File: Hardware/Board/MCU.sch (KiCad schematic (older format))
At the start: 65 parts, among them IC1 MX25LM51245GXDI00, IC2 IS66WVH8M8BLL-100B1LI_0, IC3 TSC2007, J14 52271-0679, J22 Conn_02x06_Odd_Even, J23 Conn_02x25_Odd_Even, J3 USB_B_Micro, J4 54104-4031, J5 Conn_ARM_JTAG_SWD_20, SW1 SW_Push, SW2 SW_Push, SW3 SW_Push, U17 STM32L4R9ZITx, U18 USBLC6-2SC6, U19 MOD-nRF8001, Y1 16MHz, Y2 32.768

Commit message: Alle Footprints definiert, Libs angepasst, Layout gestartet mit Plazierung, Controller und Breakout Netzmäßig getrennt.
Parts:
- removed Y1: 16MHz, symbol Device:Crystal
- added J24: Conn_01x06, Connector_PinHeader_2.54mm:PinHeader_1x06_P2.54mm_Vertical, symbol Connector_Generic:Conn_01x06
- added Y1: 16 MHz, Crystal:Crystal_SMD_3225-4Pin_3.2x2.5mm, symbol Device:Crystal_GND24
- SW1: value SW_Push -> Reset; footprint (none) -> Button_Switch_THT:SW_PUSH_6mm
- SW2: value SW_Push -> Boot; footprint (none) -> Button_Switch_THT:SW_PUSH_6mm
- SW3: value SW_Push -> Wakeup; footprint (none) -> Button_Switch_THT:SW_PUSH_6mm_H8.5mm
- Y2: footprint (none) -> Crystal:Crystal_SMD_MicroCrystal_CC7V-T1A-2Pin_3.2x1.5mm
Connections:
- net labels added: *LCD_BL_CTR, +3.3VP, PA9, PD13, PD4, PD7, VCC, VCCQ
- net labels removed: *PA9, +3.3V, +3.3VA, +VSW, GND, I2C2_SCL, I2C2_SDA, LCD_BL_CTR, LCD_BL_CTRL, LCD_LED-A, LCD_LED-K
- wire segments 514 -> 524

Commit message: Kleinigkeiten
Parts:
- IC3: symbol opendous:TSC2007 -> Womo-rescue:TSC2007-opendous

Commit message: Komplete enummerierung Geändert, Schaltplan zusammengefasst, Layout nochmals reset. BOM zu 75% fertig gestellt
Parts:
- C17: renamed from C78; footprint Capacitor_SMD:C_0603_1608Metric -> Capacitor_SMD:C_1210_3225Metric
- J5: renamed from J24; value Conn_01x06 -> Spare
- renumbered C4 to C1, C9 to C10, C10 to C11, C11 to C12, C79 to C13, C75 to C14, C76 to C15, C77 to C16, C70 to C18, C1 to C19, C5 to C2, C97 to C20, C2 to C21, C3 to C22, C12 to C23, C13 to C24, C83 to C25, C15 to C26, C98 to C27, C80 to C28, C81 to C29, C6 to C3, C82 to C30, C84 to C31, C85 to C32, C86 to C33, C100 to C34, C99 to C35, C101 to C36, C102 to C37, C7 to C4, C8 to C5, C71 to C6, C72 to C7, C73 to C8, C74 to C9, D19 to D1, FB45 to FB1, FB46 to FB2, FB49 to FB3, FB47 to FB4, FB48 to FB5, J23 to J1, J4 to J2, J14 to J3, J22 to J4, J3 to J6, J5 to J7, R75 to R1, R76 to R2, R77 to R3, R78 to R4, SW2 to SW1, SW3 to SW2, SW1 to SW3, U17 to U1, U18 to U2, U19 to U3

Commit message: Änderung des Konzeptes auf 2 Boards, eines TFT Touch mit STM32L4R9, das rein die Bedienung macht. Control Board mit STM32L476, mit noch mehr Schnittstellen. Bus zwischen Display, Board, Raspberry/ESP ist RS485, Bus als RJ45 mit Wakeup und Stromversorgung
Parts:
- removed C25, C26, C35, C36, C37: 1uF, Capacitor_SMD:C_0603_1608Metric, symbol Device:C
- removed FB1, FB2, FB3, FB4, FB5: Ferrite, Inductor_SMD:L_0603_1608Metric, symbol Device:Ferrite_Bead_Small
- removed IC3: TSC2007, Package_SO:TSSOP-16_4.4x5mm_P0.65mm, symbol Womo-rescue:TSC2007-opendous
- removed J1: Conn_02x25_Odd_Even, Connector_PinHeader_2.54mm:PinHeader_2x25_P2.54mm_Vertical, symbol Connector_Generic:Conn_02x25_Odd_Even
- removed J2: 54104-4031, SamacSys_Parts:54104-4031, symbol Womo-rescue:54104-4031-SamacSys_Parts
- removed J3: 52271-0679, SamacSys_Parts:52271-0679, symbol Womo-rescue:52271-0679-SamacSys_Parts
- removed J4: Conn_02x06_Odd_Even, Connector_PinHeader_2.54mm:PinHeader_2x06_P2.54mm_Vertical, symbol Connector_Generic:Conn_02x06_Odd_Even
- removed J5: Spare, Connector_PinHeader_2.54mm:PinHeader_1x06_P2.54mm_Vertical, symbol Connector_Generic:Conn_01x06
- removed U1: STM32L4R9ZITx, Package_QFP:LQFP-144_20x20mm_P0.5mm, symbol MCU_ST_STM32L4+:STM32L4R9ZITx
- added C?: 100nF, Capacitor_SMD:C_0603_1608Metric, symbol Device:C
- added U?: STM32L476ZGTx, Package_QFP:LQFP-144_20x20mm_P0.5mm, symbol MCU_ST_STM32L4:STM32L476ZGTx
- added U?: MAX3072E, Package_SO:SOIC-8_3.9x4.9mm_P1.27mm, symbol Interface_UART:MAX3072E
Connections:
- net labels added: +3.3V, CTRL_A, CTRL_B, GND, LIN_SEL_A0, LIN_SEL_A1, LIN_SEL_EN, SER_SEL_A0, SER_SEL_A1, SER_SEL_EN, SPI2_MISO, SPI2_MOSI, SPI2_NSS, SPI2_SCK, USART1_RTS_CTRL, USART1_RTS_DE_CTRL, USART1_RX_CTRL, USART1_TX_CTRL, USART2_RX_LIN, USART2_TX_LIN, USART3_RX_SER, USART3_TX_SER
- net labels removed: *LCD_BL_CTR, *LCD_LED-A, *LCD_LED-K, *PWR_Reset, *USART1_RX_LIN1, *USART1_TX_LIN1, *USART2_RX_LIN2, *USART2_TX_LIN2, *USART3_RX_LIN3, *USART3_TX_LIN3, LCD_37, LCD_38, LCD_39, LCD_40, LCD_B0, LCD_B1, LCD_B2, LCD_B3, LCD_B4, LCD_B5, LCD_B6, LCD_B7, LCD_CLK, LCD_DE, LCD_EN, LCD_G0, LCD_G1, LCD_G2, LCD_G3, LCD_G4, LCD_G5, LCD_G6, LCD_G7, LCD_HSYNC, LCD_INT, LCD_R0, LCD_R1, LCD_R2, LCD_R3, LCD_R4, LCD_R5, LCD_R6, LCD_R7, LCD_VSYNC, PD4, TOUCH_RESET, X+, X-, Y+, Y-
- wire segments 524 -> 349
- no-connect marks 23 -> 18
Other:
- note removed: "Connection to Mainboard"
- note removed: "I2C ADR: 1001000"
- note removed: "Touchconfig"
- note removed: "Touchcontroller"
- note removed: "Touchdisplay RGB TFT"
- moved on the sheet: C21, C22, Y1

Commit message: Display Unit Lib Fehler behoben, und noch Zeug raus geworfen Library jetzt projekt spezifisch im Hardware root.. Hauptplatine rund um den Prozessor a bissl was getan, vorbereitung Quadspi Flash und SD Karte.
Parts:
- removed IC1: MX25LM51245GXDI00, SamacSys_Parts:BGA24C100P5X5_600X800X35, symbol Womo-rescue:MX25LM51245GXDI00-SamacSys_Parts
- removed IC2: IS66WVH8M8BLL-100B1LI_0, SamacSys_Parts:BGA24C100P5X5_600X800X35, symbol Womo-rescue:IS66WVH8M8BLL-100B1LI_0-SamacSys_Parts
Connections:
- net labels added: 3VA_EN, 5V_EN, 5V_GSM_EN, 5V_Raspi_EN, CAN1_RX, CAN1_TX, I2C2_SCL, I2C2_SDA, LPUART_RTS_DE_RS485, LPUART_RX_RX485, LPUART_TX_RS485, QSPI_D0, QSPI_D1, QSPI_D2, QSPI_D3, QSPI_NCS, QSPI_SCK, Rasp_Shutdown, Rasp_down, UART5_RX, UART5_TX, uSD_CLK, uSD_D0, uSD_D1, uSD_D2, uSD_D3, uSD_Detect
- net labels removed: *CAN1_RX, *CAN1_TX, *I2C2_SCL, *I2C2_SDA, *LPUART_RTS_DE_RS485, *LPUART_RX_RX485, *LPUART_TX_RS485, *PB2, *PC6, *PC7, *Rasp_Shutdown, *Rasp_down, *UART5_RX, *UART5_TX, OctoSPI_P1_CLK, OctoSPI_P1_DQS, OctoSPI_P1_IO0, OctoSPI_P1_IO1, OctoSPI_P1_IO2, OctoSPI_P1_IO3, OctoSPI_P1_IO4, OctoSPI_P1_IO5, OctoSPI_P1_IO6, OctoSPI_P1_IO7, OctoSPI_P1_NCS, OctoSPI_P2_CLK, OctoSPI_P2_DQS, OctoSPI_P2_IO0, OctoSPI_P2_IO1, OctoSPI_P2_IO2, OctoSPI_P2_IO3, OctoSPI_P2_IO4, OctoSPI_P2_IO5, OctoSPI_P2_IO6, OctoSPI_P2_IO7, OctoSPI_P2_NCS, PD13, PD7, TOUCH_INT
- wire segments 349 -> 295
- no-connect marks 18 -> 6
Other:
- moved on the sheet: C23, C24, C27, R3, R4, Y2

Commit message: Alle Busse aus dem Prozessor geroutet, Multplexing der LIN, RS485 und TTY Busse, diverse Aufräumarbeiten.
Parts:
- removed C28, C29, C31, C32, C33, C?: 100nF, Capacitor_SMD:C_0603_1608Metric, symbol Device:C
- removed U?: MAX3072E, Package_SO:SOIC-8_3.9x4.9mm_P1.27mm, symbol Interface_UART:MAX3072E
- added C? (x2): 100nF, Capacitor_SMD:C_0603_1608Metric, symbol Device:C
- added FB? (x2): 100R, Inductor_SMD:L_0603_1608Metric, symbol Device:Ferrite_Bead_Small
- added J?: SD_Card, symbol Connector:SD_Card
- added R? (x6): 47K, Resistor_SMD:R_0603_1608Metric, symbol Device:R
- added U?: TJA1049T-3, Package_SO:SOIC-8_3.9x4.9mm_P1.27mm, symbol Interface_CAN_LIN:TJA1049T-3
- added U?: M25Q128A, Package_SO:SOIJ-8_5.3x5.3mm_P1.27mm, symbol Memory_Flash:M25PX32-VMW
- C23, C24: value 3p3 -> 4p7
- Y1: value 16 MHz -> 25 MHz
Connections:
- net labels added: +3.3VA, +5V, CTRL_H, CTRL_L, I2C1_SCL, I2C1_SDA, QSPI_CLK, RS485_SEL_A0, RS485_SEL_A1, RS485_SEL_EN, SLP-LIN1, SLP-LIN2, SLP-LIN3, SLP-LIN4, SPI3_MISO, SPI3_MOSI, SPI3_NSS, SPI3_SCK, STB-CAN, STB-CTRL, UART4_RX_GSM, UART4_TX_GSM, uSD_CMD
- net labels removed: *I2C4_SCL, *I2C4_SDA, *PF11, *UART4_RX, *UART4_TX, +3.3VP, CTRL_A, CTRL_B, PA9, QSPI_SCK, UART5_RX, UART5_TX, USART1_RTS_CTRL, USART1_RTS_DE_CTRL, VCC, VCCQ
- wire segments 295 -> 332
- no-connect marks 6 -> 2
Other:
- moved on the sheet: C1, C10, C11, C12, C13, C14, C15, C16, C17, C2, C20, C27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

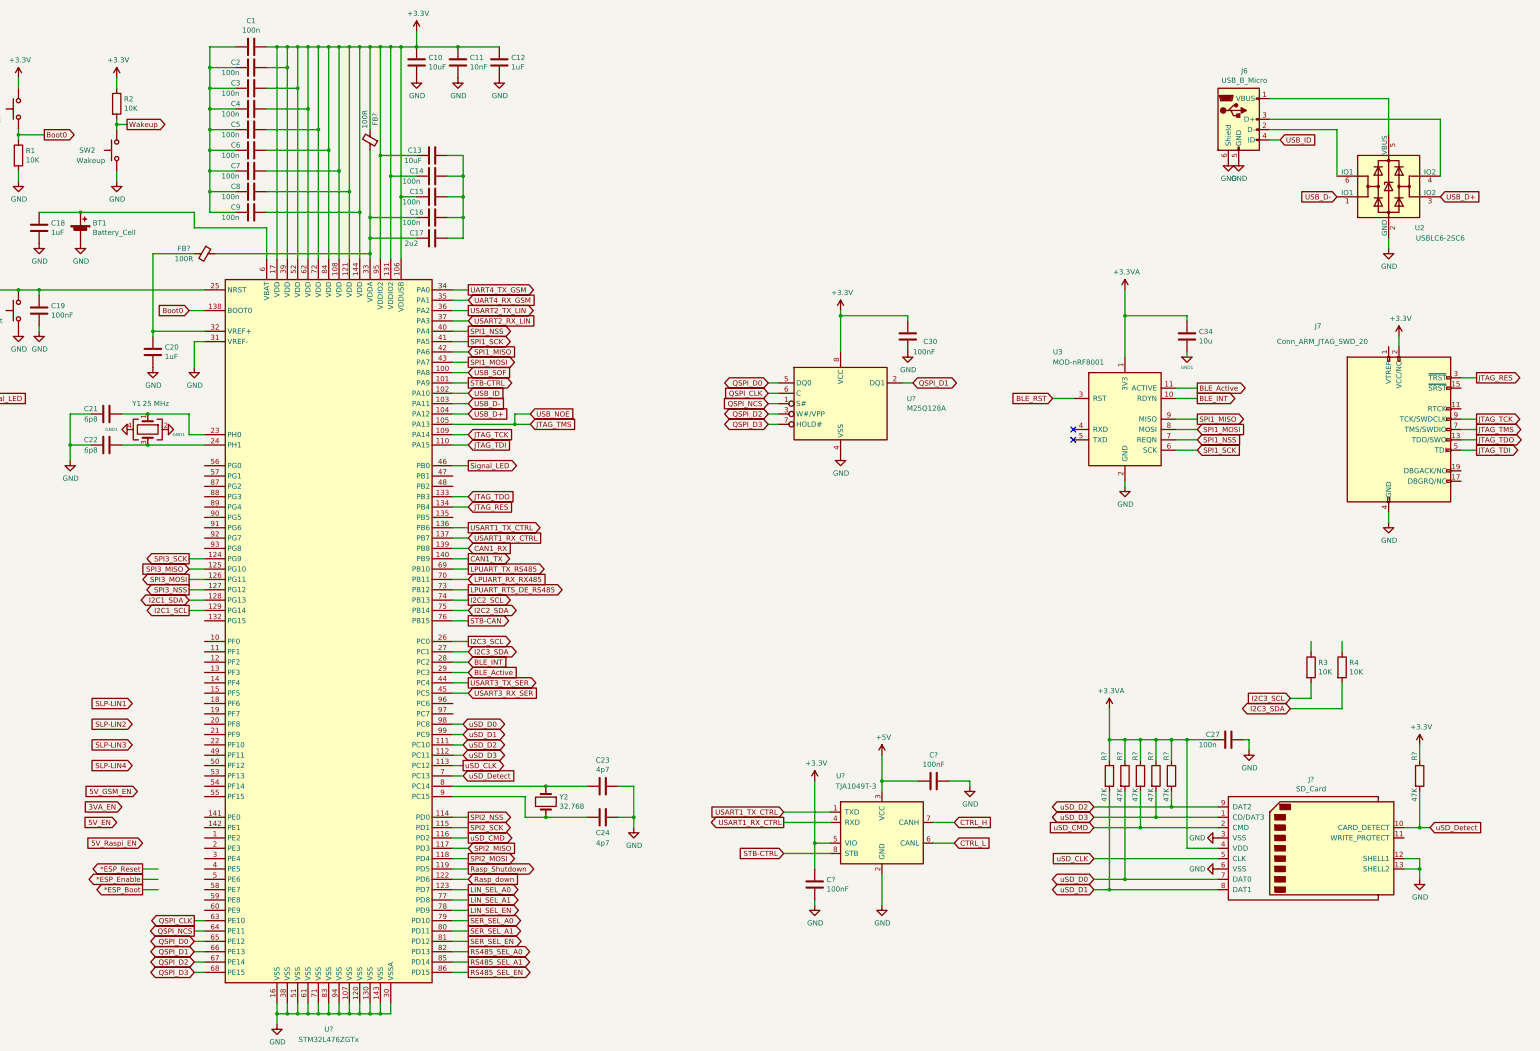
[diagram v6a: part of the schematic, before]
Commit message: Prozessor Pins zugeordnet, 4 bistabile Relais, CAN Control Interface, CAN Debug Adapter, Lagesensor zugefügt, Umwelt Sensor, ISM 868 MHz Tranceiver, ESP and Control Bus. UID Eprom. Etliche Aufräum Arbeiten.
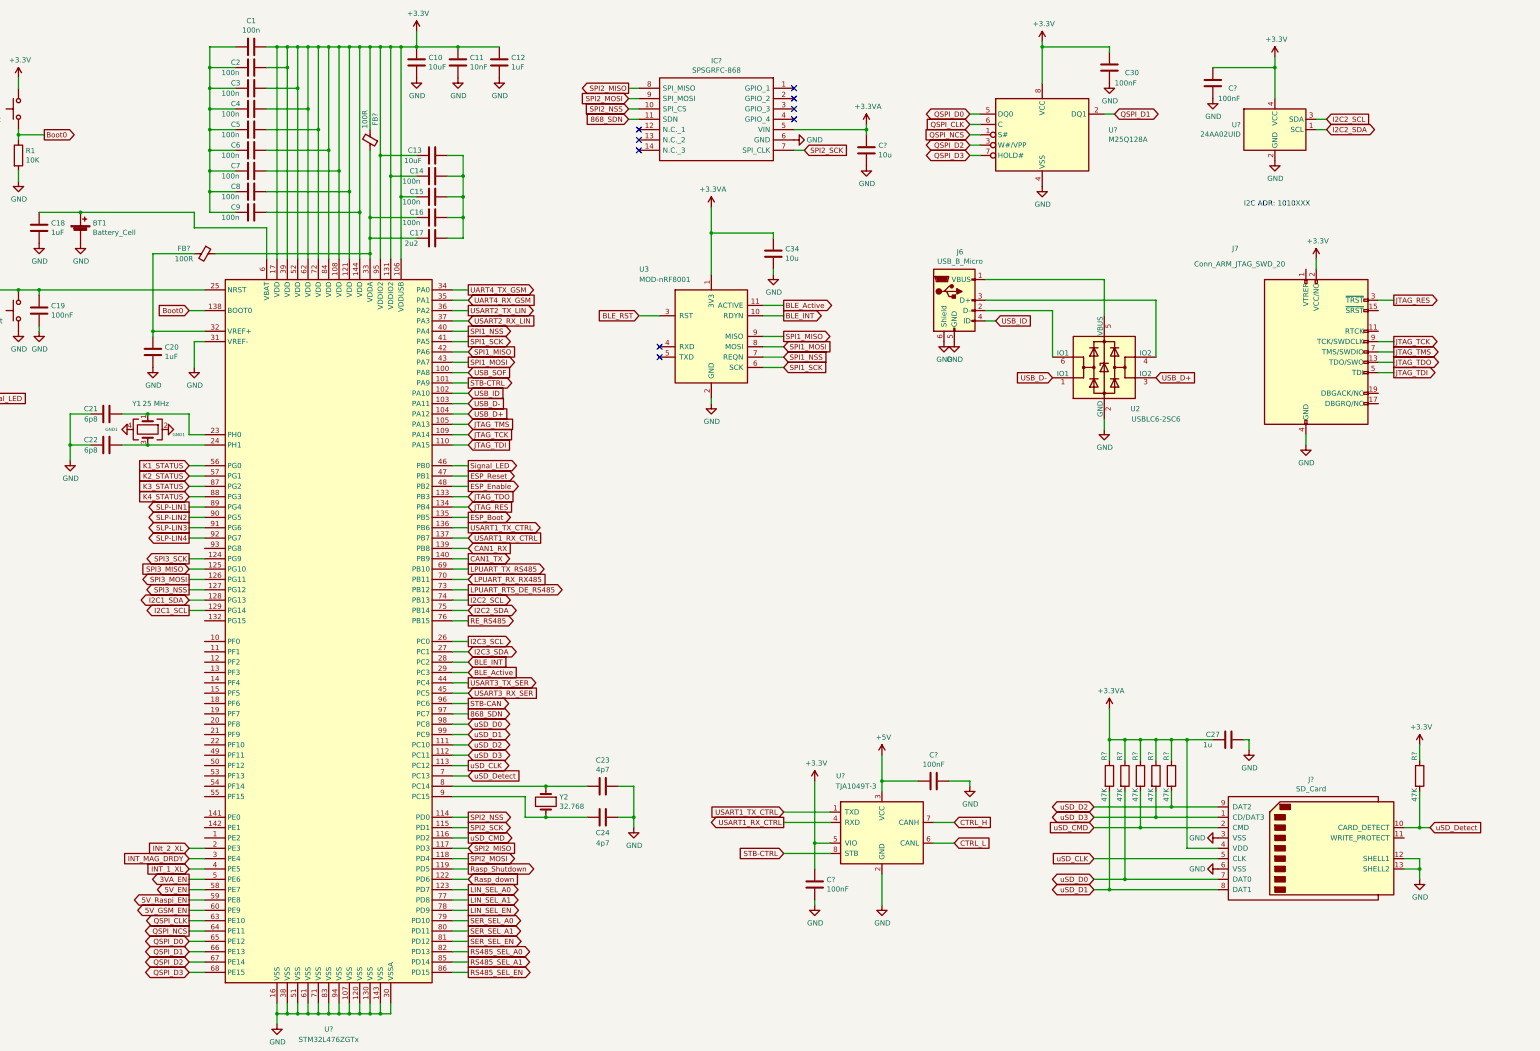
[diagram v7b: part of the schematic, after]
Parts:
- removed R2, R3, R4: 10K, Resistor_SMD:R_0603_1608Metric, symbol Device:R
- removed SW2: Wakeup, Button_Switch_THT:SW_PUSH_6mm_H8.5mm, symbol Switch:SW_Push
- added C?: 10u, Capacitor_SMD:C_1210_3225Metric, symbol Device:C
- added C?: 100nF, Capacitor_SMD:C_0603_1608Metric, symbol Device:C
- added IC?: SPSGRFC-868, SPSGRFC868, symbol Womo-Lin:SPSGRFC-868
- added U?: 24AA02UID, Package_TO_SOT_SMD:SOT-23-5, symbol Memory_EEPROM:24AA02-OT
- C27: value 100n -> 1u
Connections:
- net +3.3VA: now also C?.1, IC?.5 (VIN)
- net +3V3: now also C?.1, U?.4 (VCC)
- net 3VA_EN: now also U?.5 (PE6)
- net 5V_EN: now also U?.58 (PE7)
- net 5V_GSM_EN: now also U?.60 (PE9)
- net 5V_Raspi_EN: now also U?.59 (PE8)
- net GND: now also C34.2, C?.2, C?.2, IC?.6 (GND), U?.2 (GND)
- net GND1: no longer C34.2
- net I2C2_SCL: now also U?.3 (SDA)
- net I2C2_SDA: now also U?.1 (SCL)
- net SLP-LIN1: now also U?.89 (PG4)
- net SLP-LIN2: now also U?.90 (PG5)
- net SLP-LIN3: now also U?.91 (PG6)
- net SLP-LIN4: now also U?.92 (PG7)
- net SPI2_MISO: now also IC?.8 (SPI_MISO)
- net SPI2_MOSI: now also IC?.9 (SPI_MOSI)
- net SPI2_NSS: now also IC?.10 (SPI_CS)
- net SPI2_SCK: now also IC?.7 (SPI_CLK)
- net STB-CAN: now also U?.96 (PC6); no longer U?.76 (PB15)
- net ESP_Boot: now reaches U?.135 (PB5)
- net INt_2_XL: now reaches U?.2 (PE3)
- net INT_MAG_DRDY: now reaches U?.3 (PE4)
- net INT_1_XL: now reaches U?.4 (PE5)
- net ESP_Reset: now reaches U?.47 (PB1)
- net ESP_Enable: now reaches U?.48 (PB2)
- net K1_STATUS: now reaches U?.56 (PG0)
- net K2_STATUS: now reaches U?.57 (PG1)
- net K3_STATUS: now reaches U?.87 (PG2)
- net K4_STATUS: now reaches U?.88 (PG3)
- net 868_SDN: now reaches U?.97 (PC7)
- net 868_SDN: now also IC?.11 (SDN)
- new net RE_RS485: U?.76 (PB15)
- no-connect marks 2 -> 9
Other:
- note added: "I2C ADR: 1010XXX"
- moved on the sheet: C30, C34, J6, J7, U2, U3, U?

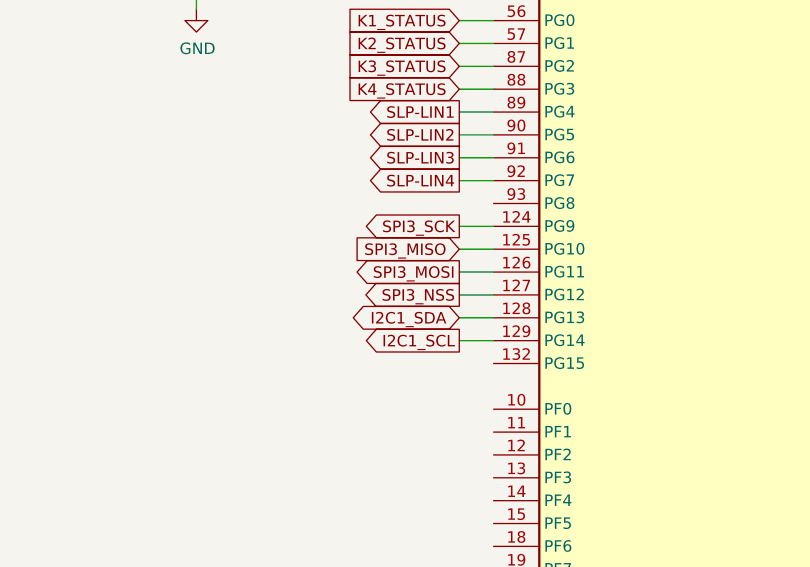
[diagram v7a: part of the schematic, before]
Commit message: Lib Update, Relais Treiber hinzugefügt, Kleinkram
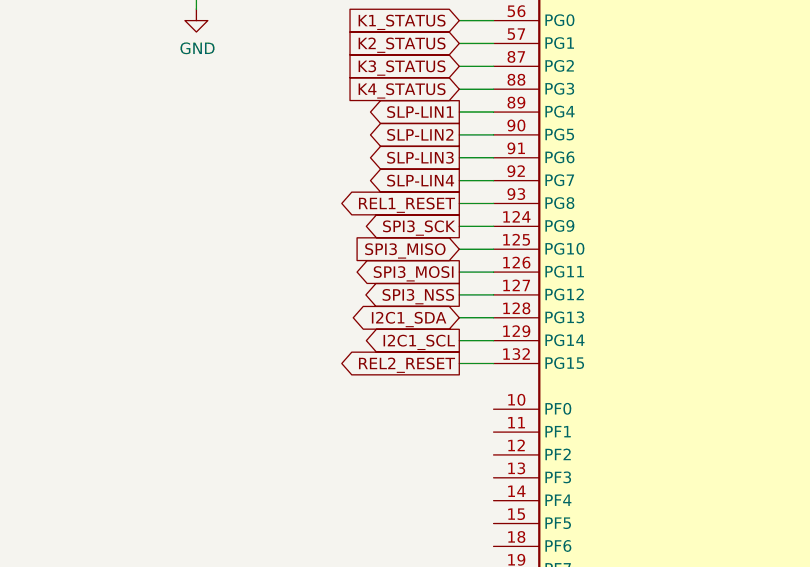
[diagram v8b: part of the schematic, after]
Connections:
- net REL2_RESET: now reaches U?.132 (PG15)
- net REL1_RESET: now reaches U?.93 (PG8)
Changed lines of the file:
@@
 Wire Wire Line
 	3050 5650 3200 5650
+Text GLabel 3050 5750 0    50   Output ~ 0
+REL1_RESET
+Text GLabel 3050 6450 0    50   Output ~ 0
+REL2_RESET
+Wire Wire Line
+	3200 5750 3050 5750
+Wire Wire Line
+	3200 6450 3050 6450
 $EndSCHEMATC
